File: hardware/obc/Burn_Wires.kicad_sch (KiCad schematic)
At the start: 28 parts, among them Q501 MMBT2222AT, Q502 IRLML2803, Q503 IRLML2803, Q504 IRLML2803, Q505 IRF7406PbF, Q506 IRF7406PbF, Q507 IRF7406PbF, U501 PE014006

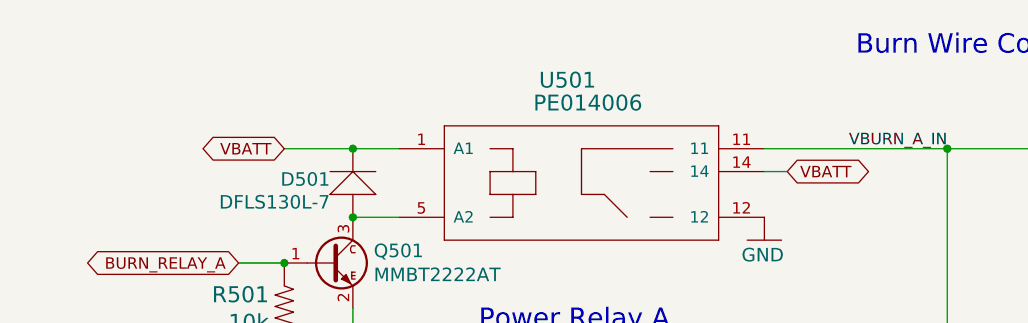
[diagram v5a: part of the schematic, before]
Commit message: obc: preliminary board layout
Entered design rules and grouped components according to schematic. Slightly edited BOM.
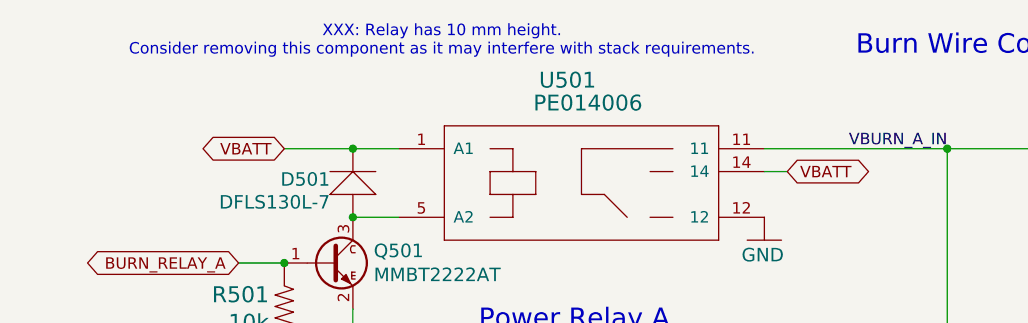
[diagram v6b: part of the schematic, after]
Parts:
- U501: DNI (none) -> NP_JLC; LCSC C1563209 -> (none); Notes (Potentially) Not placed by JLCPCB -> (none)
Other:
- note added: "XXX: Relay has 10 mm height. Consider removing this component as it may interfere with stack requirements."
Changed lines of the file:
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@@
+		)
+	)
+	(text "XXX: Relay has 10 mm height.\nConsider removing this component as it may interfere with stack requirements."
+		(exclude_from_sim no)
+		(at 68.326 18.542 0)
+		(effects
+			(font
+				(size 1.27 1.27)
+			)
 		)
 	)
@@
 			)
 		)
-		(property "LCSC" "C1563209"
+		(property "LCSC" ""
 			(at 81.28 33.02 0)
 			(effects
@@
 			)
 		)
-		(property "Notes" "(Potentially) Not placed by JLCPCB"
+		(property "Notes" ""
 			(at 81.28 33.02 0)
 			(effects
@@
 			(at 81.28 33.02 0)
 			(effects
+				(font
+					(size 1.27 1.27)
+				)
+				(hide yes)
+			)
+		)
+		(property "DNI" "NP_JLC"
+			(at 81.28 33.02 0)
+			(effects

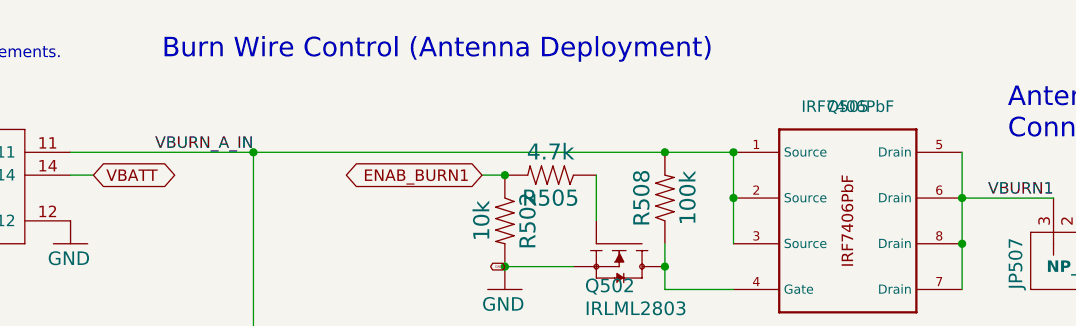
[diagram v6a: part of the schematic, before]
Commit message: obc: formal placement and 3D models entered
Placed components of onto board, orienting them for ease of trace creation. Entered 3D models of footprints into KiCad for design verification and aesthetics.
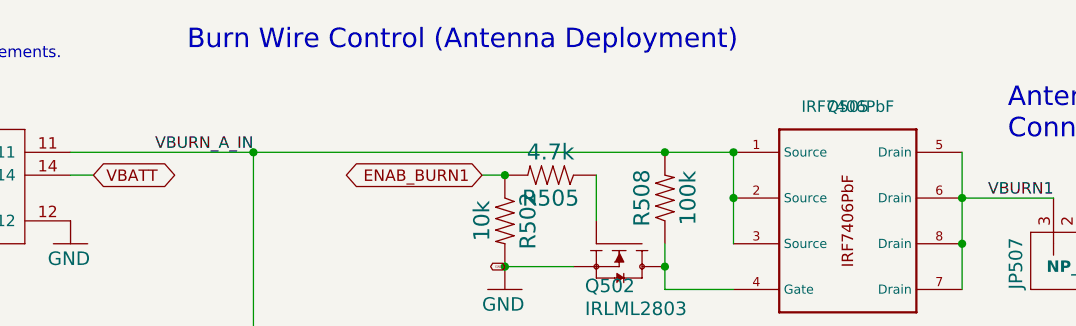
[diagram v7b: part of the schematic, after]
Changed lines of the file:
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@@
 	(text "Burn Wire Control (Antenna Deployment)"
 		(exclude_from_sim no)
-		(at 114.3 20.32 0)
+		(at 117.094 19.304 0)
 		(effects
 			(font

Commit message: obc: component reorganization
Blanket shrunk silk text, edited connector placement, switched out molex connectors, entered step files, and reorganized to increase area-efficiency.
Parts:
- JP501, JP502, JP503, JP504, JP505, JP506, JP507, JP508, JP509: footprint mainboard:MOLEX-1X3_LOCK -> SSE_Footprints:CONN_22-11-2032_MOL; Manufacturer_Part_Number 22-23-2037 -> 0022112032
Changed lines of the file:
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@@
 			)
 		)
-		(property "Footprint" "mainboard:MOLEX-1X3_LOCK"
+		(property "Footprint" "SSE_Footprints:CONN_22-11-2032_MOL"
 			(at 215.9 67.31 0)
 			(effects
@@
 			)
 		)
-		(property "Datasheet" "https://www.mouser.com/datasheet/2/276/022232037_sd-589157.pdf"
+		(property "Datasheet" "https://tools.molex.com/pdm_docs/sd/022112032_sd.pdf"
 			(at 215.9 67.31 0)
 			(effects
@@
 			)
 		)
-		(property "Manufacturer_Part_Number" "22-23-2037"
+		(property "Manufacturer_Part_Number" "	 0022112032"
 			(at 207.518 69.85 0)
 			(effects
@@
 			)
 		)
-		(property "Footprint" "mainboard:MOLEX-1X3_LOCK"
+		(property "Footprint" "SSE_Footprints:CONN_22-11-2032_MOL"
 			(at 215.9 43.18 0)
 			(effects
@@
 			)
 		)
-		(property "Datasheet" "https://www.mouser.com/datasheet/2/276/022232037_sd-589157.pdf"
+		(property "Datasheet" "https://tools.molex.com/pdm_docs/sd/022112032_sd.pdf"
 			(at 215.9 43.18 0)
 			(effects
@@
 			)
 		)
-		(property "Manufacturer_Part_Number" "22-23-2037"
+		(property "Manufacturer_Part_Number" "	 0022112032"
 			(at 207.518 45.72 0)
 			(effects
@@
 			)
 		)
-		(property "Footprint" "mainboard:MOLEX-1X3_LOCK"
+		(property "Footprint" "SSE_Footprints:CONN_22-11-2032_MOL"
 			(at 35.56 158.75 0)
 			(effects
@@
 			)
 		)
-		(property "Datasheet" "https://www.mouser.com/datasheet/2/276/022232037_sd-589157.pdf"
+		(property "Datasheet" "https://tools.molex.com/pdm_docs/sd/022112032_sd.pdf"
 			(at 35.56 158.75 0)
 			(effects
@@
 			)
 		)
-		(property "Manufacturer_Part_Number" "22-23-2037"
+		(property "Manufacturer_Part_Number" "	 0022112032"
 			(at 27.178 161.29 0)
 			(effects
@@
 			)
 		)
-		(property "Footprint" "mainboard:MOLEX-1X3_LOCK"
+		(property "Footprint" "SSE_Footprints:CONN_22-11-2032_MOL"
 			(at 31.75 127 0)
 			(effects
@@
 			)
 		)
-		(property "Datasheet" "https://www.mouser.com/datasheet/2/276/022232037_sd-589157.pdf"
+		(property "Datasheet" "https://tools.molex.com/pdm_docs/sd/022112032_sd.pdf"
 			(at 31.75 127 0)
 			(effects
@@
 			)
 		)
-		(property "Manufacturer_Part_Number" "22-23-2037"
+		(property "Manufacturer_Part_Number" "	 0022112032"
 			(at 29.21 118.618 0)
 			(effects
@@
 			)
 		)
-		(property "Footprint" "mainboard:MOLEX-1X3_LOCK"
+		(property "Footprint" "SSE_Footprints:CONN_22-11-2032_MOL"
 			(at 215.9 92.71 0)
 			(effects
@@
 			)
 		)
-		(property "Datasheet" "https://www.mouser.com/datasheet/2/276/022232037_sd-589157.pdf"
+		(property "Datasheet" "https://tools.molex.com/pdm_docs/sd/022112032_sd.pdf"
 			(at 215.9 92.71 0)
 			(effects
@@
 			)
 		)
-		(property "Manufacturer_Part_Number" "22-23-2037"
+		(property "Manufacturer_Part_Number" "	 0022112032"
 			(at 207.518 95.25 0)
 			(effects
@@
 			)
 		)
-		(property "Footprint" "mainboard:MOLEX-1X3_LOCK"
+		(property "Footprint" "SSE_Footprints:CONN_22-11-2032_MOL"
 			(at 74.93 158.75 0)
 			(effects
@@
 			)
 		)
-		(property "Datasheet" "https://www.mouser.com/datasheet/2/276/022232037_sd-589157.pdf"
+		(property "Datasheet" "https://tools.molex.com/pdm_docs/sd/022112032_sd.pdf"
 			(at 74.93 158.75 0)
 			(effects
@@
 			)
 		)
-		(property "Manufacturer_Part_Number" "22-23-2037"
+		(property "Manufacturer_Part_Number" "	 0022112032"
 			(at 66.548 161.29 0)
 			(effects
@@
 			)
 		)
-		(property "Footprint" "mainboard:MOLEX-1X3_LOCK"
+		(property "Footprint" "SSE_Footprints:CONN_22-11-2032_MOL"
 			(at 115.57 160.02 0)
 			(effects
@@
 			)
 		)
-		(property "Datasheet" "https://www.mouser.com/datasheet/2/276/022232037_sd-589157.pdf"
+		(property "Datasheet" "https://tools.molex.com/pdm_docs/sd/022112032_sd.pdf"
 			(at 115.57 160.02 0)
 			(effects
@@
 			)
 		)
-		(property "Manufacturer_Part_Number" "22-23-2037"
+		(property "Manufacturer_Part_Number" "	 0022112032"
 			(at 107.188 162.56 0)
 			(effects
@@
 			)
 		)
-		(property "Footprint" "mainboard:MOLEX-1X3_LOCK"
+		(property "Footprint" "SSE_Footprints:CONN_22-11-2032_MOL"
 			(at 111.76 127 0)
 			(effects
@@
 			)
 		)
-		(property "Datasheet" "https://www.mouser.com/datasheet/2/276/022232037_sd-589157.pdf"
+		(property "Datasheet" "https://tools.molex.com/pdm_docs/sd/022112032_sd.pdf"
 			(at 111.76 127 0)
 			(effects
@@
 			)
 		)
-		(property "Manufacturer_Part_Number" "22-23-2037"
+		(property "Manufacturer_Part_Number" "	 0022112032"
 			(at 109.22 118.618 0)
 			(effects
@@
 			)
 		)
-		(property "Footprint" "mainboard:MOLEX-1X3_LOCK"
+		(property "Footprint" "SSE_Footprints:CONN_22-11-2032_MOL"
 			(at 72.39 127 0)
 			(effects
@@
 			)
 		)
-		(property "Datasheet" "https://www.mouser.com/datasheet/2/276/022232037_sd-589157.pdf"
+		(property "Datasheet" "https://tools.molex.com/pdm_docs/sd/022112032_sd.pdf"
 			(at 72.39 127 0)
 			(effects
@@
 			)
 		)
-		(property "Manufacturer_Part_Number" "22-23-2037"
+		(property "Manufacturer_Part_Number" "	 0022112032"
 			(at 69.85 118.618 0)
 			(effects
